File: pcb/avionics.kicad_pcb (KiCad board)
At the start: 2 copper layers, 100 x 48 mm, 108 parts, among them IC101 STM32F405VGT, IC102 ADP3335, IC201 MAX-7Q, IC701 ADXL345, IC702 L3G4200D, IC703 MS5611-01BA03, IC704 HMC5883L, P101 CONN_01X02, P102 CONN_01X04, P103 SWD, P201 SMA, P202 SMA, P501 CONN_01X02, P502 CONN_01X02, P503 CONN_01X02, P504 CONN_01X02, Q501 IRF7910, Q502 FDN304P, Q503 FDN304P, Q504 IRF7910, Q505 FDN304P, Q506 FDN304P, Q601 IRF7910, U202 RFM69W, U401 MICROSD_HOLDER, X101 8M

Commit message: Tried to route a little more of the board. Are the jumps ok?
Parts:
- moved R403 11.4 mm to (113.9, 49.8)
- moved R402 10.6 mm to (129.5, 49.7)
- moved C109 10.5 mm to (136.0, 62.8)
- moved R404 10.4 mm to (113.9, 52.3), turned to 270 degrees
- moved C111 10.2 mm to (146.6, 56.8), turned to 90 degrees
- moved C103 9.96 mm to (136.0, 58.6)
- moved C110 9.56 mm to (136.0, 60.0)
- moved C108 9.49 mm to (145.2, 68.5)
- moved R401 9.02 mm to (129.5, 52.2), turned to 270 degrees
- moved D604 8.81 mm to (147.7, 43.5), turned to 0 degrees
- moved C703 8.75 mm to (158.9, 75.9), turned to 180 degrees
- moved C104 8.44 mm to (145.2, 67.1)
- moved C401 8.42 mm to (129.5, 54.7)
- moved C102 8.24 mm to (136.0, 68.4)
- moved R604 8.10 mm to (145.2, 43.5), turned to 0 degrees
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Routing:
- net GND: track 8.87 -> 90.0 mm, vias 0 -> 14
- net +3V3: track 10.9 -> 61.8 mm
- net /Datalogging & Pyros/µSD_DAT0: track 0.00 -> 29.7 mm
- net /Datalogging & Pyros/~PY4_CHK: track 0.00 -> 27.2 mm
- net /Inertial Measurement/GYRO_SDA: track 0.00 -> 24.8 mm
- net /Datalogging & Pyros/µSD_CMD: track 0.00 -> 22.5 mm
- net /Datalogging & Pyros/PY4_TRG: track 0.00 -> 21.5 mm
- net /Datalogging & Pyros/µSD_DAT1: track 0.00 -> 20.4 mm
- net /Datalogging & Pyros/~PY1_CHK: track 0.00 -> 16.9 mm, vias 0 -> 2
- net /Datalogging & Pyros/~PY2_CHK: track 0.00 -> 16.8 mm, vias 0 -> 2
- net /Datalogging & Pyros/~PY3_CHK: track 0.00 -> 15.8 mm, vias 0 -> 2
- net /Datalogging & Pyros/PY3_TRG: track 0.00 -> 14.0 mm
- net /Inertial Measurement/GYRO_SCL: track 0.00 -> 13.6 mm
- net /Datalogging & Pyros/~IMU_OK: track 0.00 -> 13.4 mm
- net /Inertial Measurement/ACCEL_CS: track 0.00 -> 12.9 mm, vias 0 -> 2
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
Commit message: routing after today's meeting
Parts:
- added M3_MOUNT: VAL**, avionics14:M3_MOUNT, F.Cu at (158.5, 85.0)
- added M3_MOUNT: VAL**, avionics14:M3_MOUNT, F.Cu at (158.5, 45.0)
- added M3_MOUNT: VAL**, avionics14:M3_MOUNT, F.Cu at (92.4, 43.6)
- added M3_MOUNT: VAL**, avionics14:M3_MOUNT, F.Cu at (92.1, 85.1)
- moved C708 18.9 mm to (142.3, 37.1)
- moved IC703 18.9 mm to (140.5, 37.8)
- moved R706 18.9 mm to (142.3, 34.6)
- moved C105 15.2 mm to (149.6, 54.7), turned to 90 degrees
- moved C114 11.3 mm to (132.9, 53.3), turned to 90 degrees
- moved C704 9.43 mm to (128.5, 82.1)
- moved C707 9.43 mm to (131.0, 76.3)
- moved C706 9.43 mm to (133.5, 76.3)
- moved R701 9.43 mm to (127.9, 79.6)
- moved R702 9.43 mm to (127.2, 82.1)
- moved C702 9.43 mm to (129.9, 83.3)
- moved IC702 9.43 mm to (129.4, 78.5)
- moved R704 9.43 mm to (129.2, 76.5)
- moved Q601 7.77 mm to (154.2, 79.5)
- moved C109 7.31 mm to (131.3, 68.4), turned to 90 degrees
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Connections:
- IC101 pad 38: /Datalogging & Pyros/PY1_TRG -> /Datalogging & Pyros/~PY1_CHK
- IC101 pad 39: /Datalogging & Pyros/PY2_TRG -> /Datalogging & Pyros/PY1_TRG
- IC101 pad 40: /Datalogging & Pyros/PY3_TRG -> /Datalogging & Pyros/PY2_TRG
- IC101 pad 41: /Datalogging & Pyros/PY4_TRG -> /Datalogging & Pyros/~PY2_CHK
- IC101 pad 42: /Datalogging & Pyros/~PY1_CHK -> /Datalogging & Pyros/~PY3_CHK
- IC101 pad 43: /Datalogging & Pyros/~PY2_CHK -> /Datalogging & Pyros/PY3_TRG
- IC101 pad 44: /Datalogging & Pyros/~PY3_CHK -> /Datalogging & Pyros/PY4_TRG
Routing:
- net +3V3: track 61.8 -> 86.7 mm
- net /EXT_TX: track 0.00 -> 24.0 mm
- net /EXT_RX: track 0.00 -> 23.0 mm
- net /Inertial Measurement/GYRO_SDA: track 24.8 -> 6.43 mm
- net /Datalogging & Pyros/~PY1_CHK: track 16.9 -> 0.45 mm, vias 2 -> 0
- net /Inertial Measurement/GYRO_SCL: track 13.6 -> 1.72 mm
- net /Datalogging & Pyros/PY2_TRG: track 10.4 -> 0.00 mm
- net /Radio/RADIO_MOSI: track 0.00 -> 9.20 mm
- net /Radio/RADIO_IRQ: track 0.00 -> 9.18 mm
- net /Radio/RADIO_CS: track 0.00 -> 9.16 mm
- net /Radio/RADIO_CLK: track 0.00 -> 9.12 mm
- net /Radio/RADIO_MISO: track 0.00 -> 9.00 mm
- net /Inertial Measurement/GYRO_DRDY: track 11.3 -> 2.40 mm
- net Net-(ABI-042-RC601-Pad2): track 8.14 -> 16.5 mm
- net /Datalogging & Pyros/PY1_TRG: track 7.79 -> 0.00 mm, vias 2 -> 0
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- removed copper zone on B.Cu, net GND
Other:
- net class Default: via_dia 1 -> 0.8; via_drill 0.6 -> 0.4
- rule via_min_drill: 0.6 -> 0.4
- rule via_min_size: 1 -> 0.8

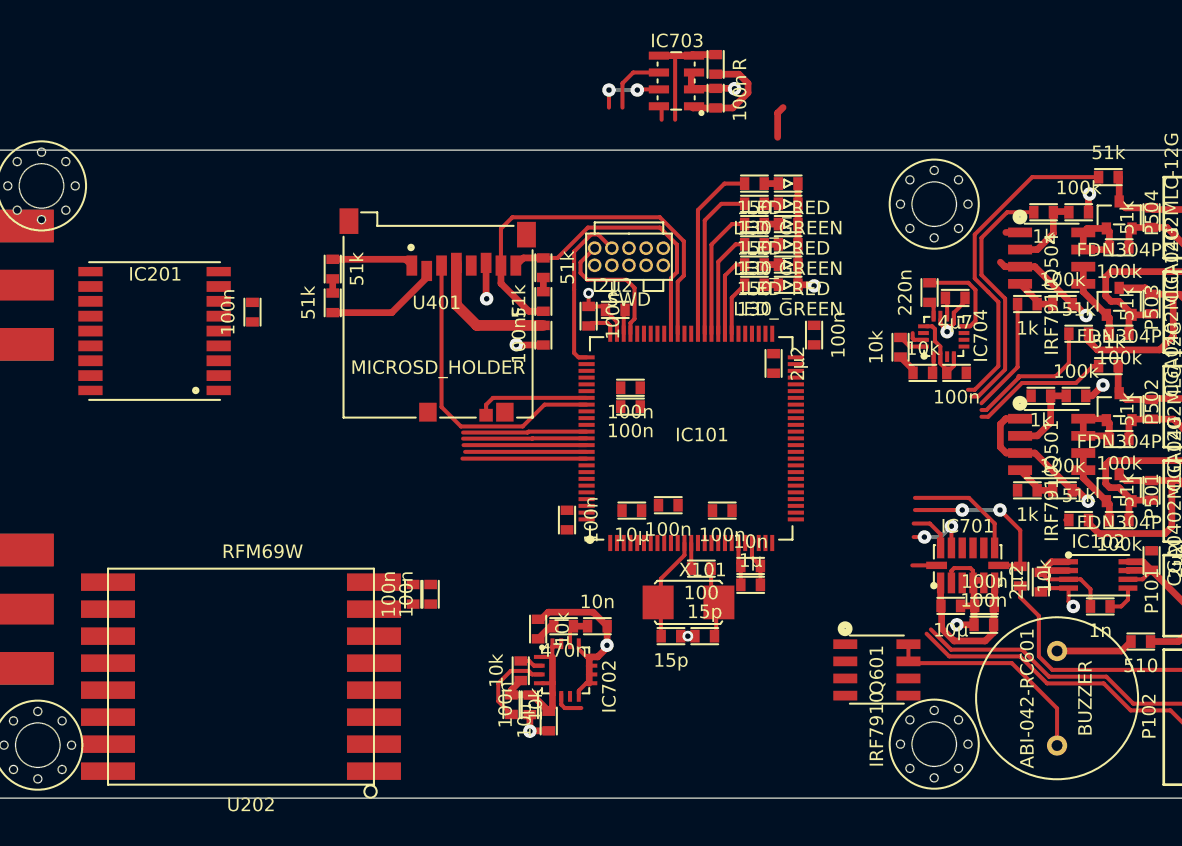
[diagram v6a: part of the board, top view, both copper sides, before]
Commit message: Have continued routing the PCB. I have tried to make it more compact on the right side of the PCB. It is still possible to push it more togheter by moving the microcontroller into the gap to its right, but then  we may have reroute certain adjacent components.
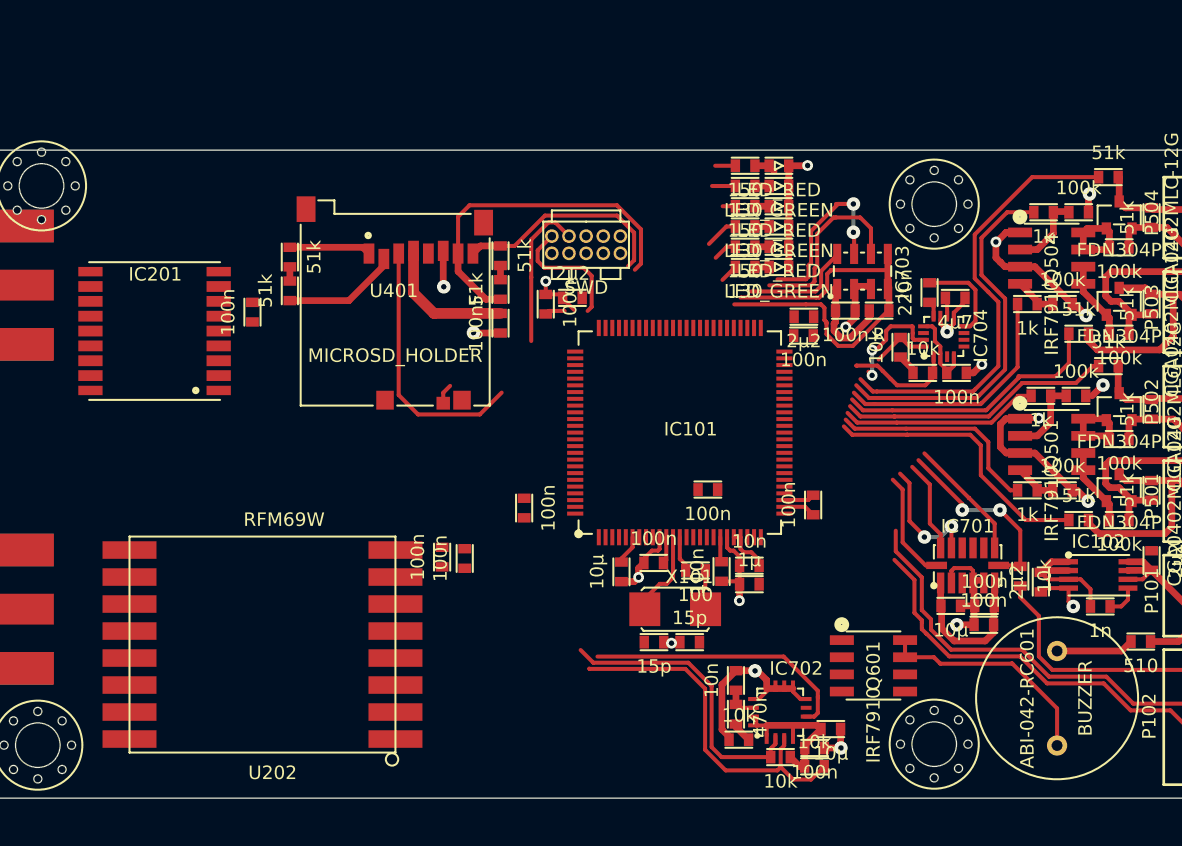
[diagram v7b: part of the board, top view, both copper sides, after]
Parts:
- moved R702 22.9 mm to (149.6, 86.6), turned to 180 degrees
- moved R706 21.9 mm to (154.4, 52.9), turned to 0 degrees
- moved C704 21.3 mm to (149.6, 85.3), turned to 0 degrees
- moved C702 20.9 mm to (150.8, 83.9), turned to 0 degrees
- moved R701 20.3 mm to (147.1, 86.0), turned to 0 degrees
- moved C708 18.4 mm to (151.9, 52.9), turned to 0 degrees
- moved IC702 17.6 mm to (146.1, 84.4), turned to 90 degrees
- moved IC703 17.2 mm to (151.3, 51.1), turned to 90 degrees
- moved R704 17.0 mm to (144.0, 84.7), turned to 180 degrees
- moved C707 14.3 mm to (143.8, 82.8), turned to 90 degrees
- moved C110 11.7 mm to (137.7, 71.6), turned to 180 degrees
- moved C706 11.0 mm to (143.8, 80.3), turned to 270 degrees
- moved C103 9.47 mm to (141.7, 66.1)
- moved C112 6.74 mm to (149.5, 67.3), turned to 270 degrees
- moved C102 6.30 mm to (142.7, 72.2), turned to 270 degrees
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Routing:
- net /Inertial Measurement/BARO_CS: track 8.78 -> 31.4 mm
- net /Datalogging & Pyros/~PY1_CHK: track 0.45 -> 21.3 mm
- net /Inertial Measurement/GYRO_SDA: track 6.43 -> 26.5 mm
- net /Inertial Measurement/GYRO_SCL: track 1.72 -> 21.7 mm
- net /Inertial Measurement/GYRO_DRDY: track 2.40 -> 20.2 mm
- net GND: track 91.0 -> 108.4 mm, vias 15 -> 20
- net /Datalogging & Pyros/PY1_TRG: track 0.00 -> 16.0 mm
- net /Datalogging & Pyros/PY2_TRG: track 0.00 -> 14.7 mm
- net /Datalogging & Pyros/~IMU_OK: track 13.4 -> 1.50 mm
- net /Datalogging & Pyros/IMU_OK: track 11.9 -> 1.73 mm
- net /Datalogging & Pyros/~PY2_CHK: track 10.3 -> 20.4 mm
- net /Datalogging & Pyros/~PY3_CHK: track 10.2 -> 20.1 mm
- net /Datalogging & Pyros/PY3_TRG: track 8.46 -> 18.3 mm
- net /Inertial Measurement/BARO_MOSI: track 5.22 -> 15.0 mm
- net /Radio/RADIO_MOSI: track 9.20 -> 0.00 mm
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
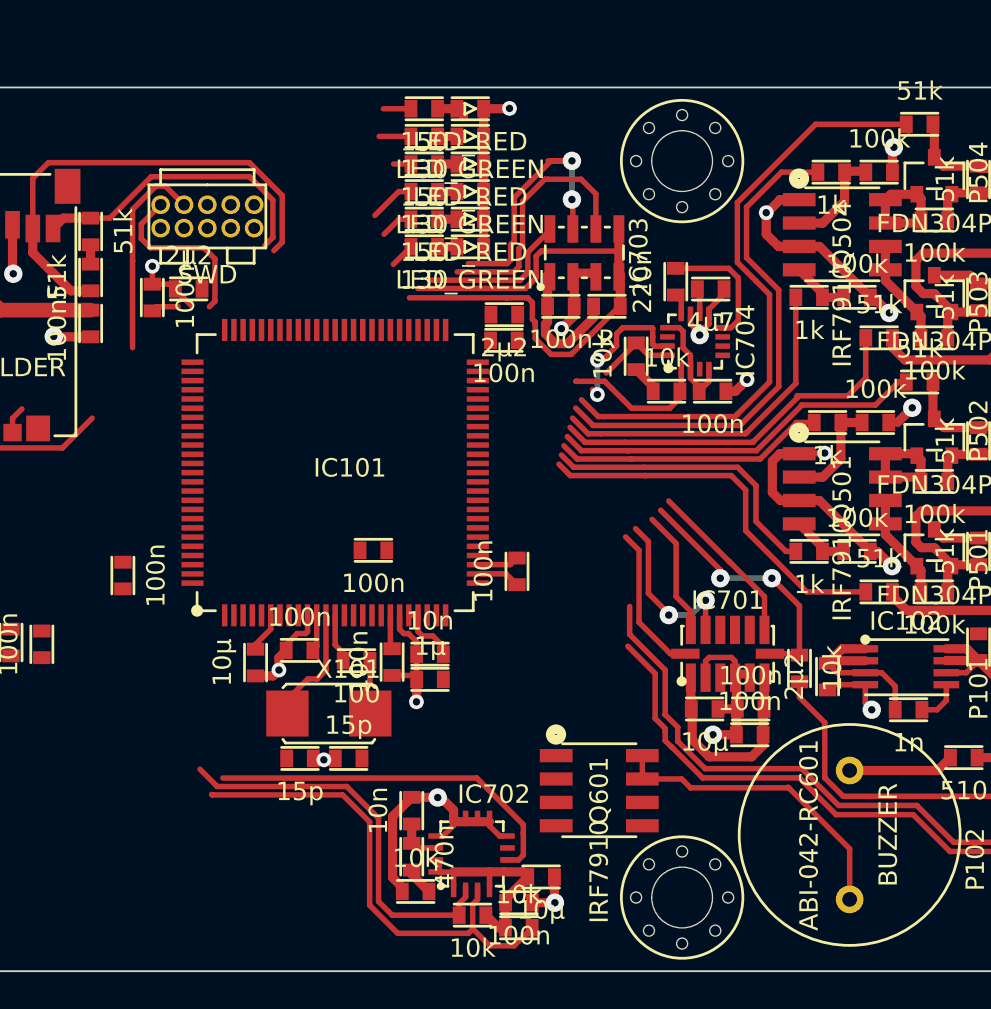
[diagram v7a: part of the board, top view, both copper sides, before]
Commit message: moved the microprosessor closer to the right. If we rethink the bottom part of the circuit board we could possibly move it even further. If we want to do that we should probably get on with it as soon as possible so we don't have to redo too much of the routing.
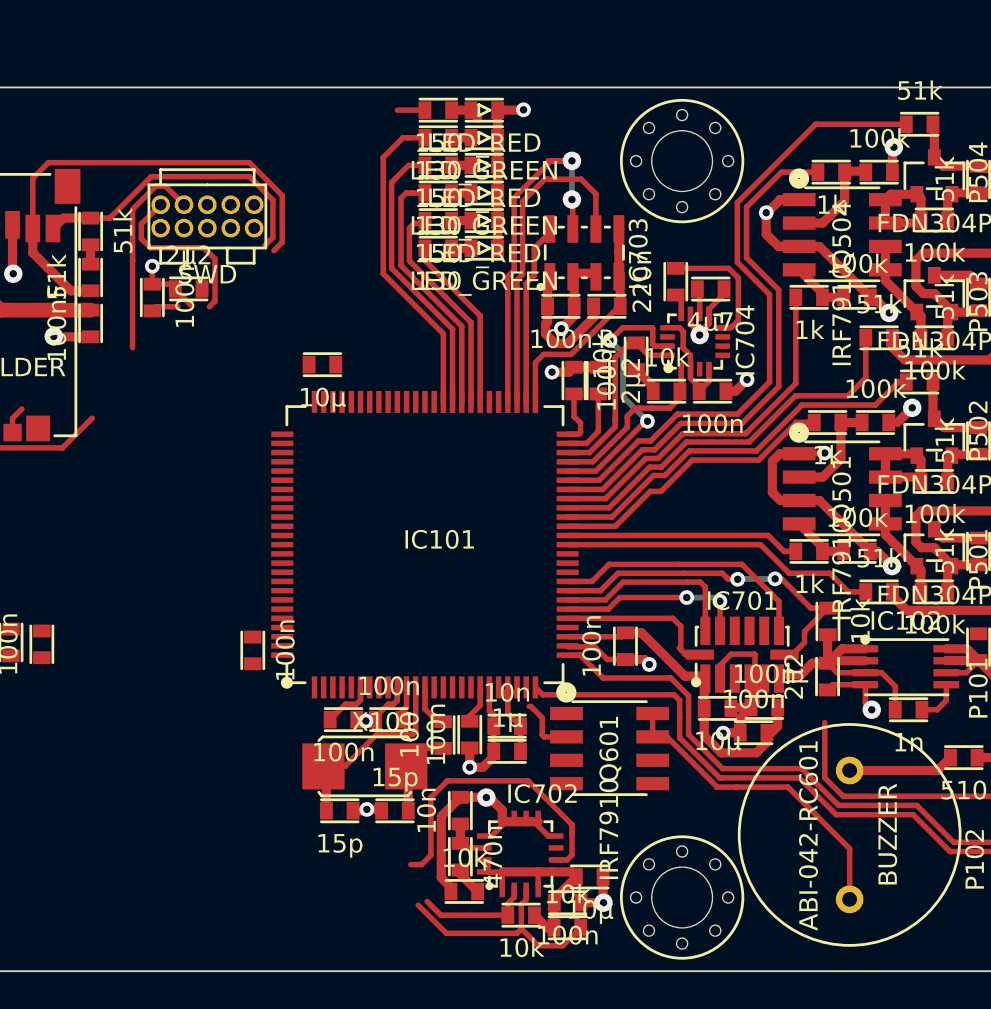
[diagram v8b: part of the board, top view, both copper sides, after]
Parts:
- moved C101 16.6 mm to (139.0, 56.1), turned to 0 degrees
- moved C103 9.34 mm to (140.1, 75.3)
- moved C109 8.14 mm to (135.2, 71.6)
- moved C112 7.16 mm to (155.4, 71.3)
- moved IC101 6.25 mm to (138.5, 73.6)
- moved C111 6.24 mm to (153.9, 56.9), turned to 90 degrees
- moved R101 6.20 mm to (145.5, 76.2), turned to 270 degrees
- moved C110 6.14 mm to (142.6, 75.3)
- moved C102 5.77 mm to (147.0, 76.1)
- moved C104 5.73 mm to (149.0, 77.1)
- moved C108 5.73 mm to (149.0, 75.7)
- moved C105 4.39 mm to (152.6, 56.9), turned to 90 degrees
- moved C107 3.80 mm to (142.9, 80.3)
- moved C106 3.57 mm to (139.9, 80.3)
- moved X101 3.47 mm to (139.2, 77.9)
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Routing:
- net /Inertial Measurement/BARO_CS: track 31.4 -> 12.0 mm
- net /Datalogging & Pyros/IMU_OK: track 1.73 -> 17.3 mm
- net /Inertial Measurement/GYRO_SCL: track 21.7 -> 6.40 mm
- net /Datalogging & Pyros/~RADIO_OK: track 0.94 -> 15.5 mm
- net /Inertial Measurement/GYRO_SDA: track 26.5 -> 12.8 mm
- net /Datalogging & Pyros/RADIO_OK: track 2.49 -> 13.9 mm
- net +3V3: track 93.4 -> 103.7 mm
- net /Datalogging & Pyros/~PY_OK: track 1.79 -> 11.8 mm
- net /Datalogging & Pyros/PY_OK: track 1.35 -> 9.59 mm
- net /Inertial Measurement/MAGNO_DRDY: track 8.33 -> 15.2 mm
- net /Inertial Measurement/MAGNO_SDA: track 4.51 -> 10.8 mm
- net /Inertial Measurement/BARO_MOSI: track 15.0 -> 20.4 mm
- net /Inertial Measurement/ACCEL_INT: track 9.36 -> 14.5 mm
- net /Inertial Measurement/ACCEL_CS: track 14.5 -> 19.3 mm
- net GND: track 108.4 -> 112.5 mm, vias 20 -> 22
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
